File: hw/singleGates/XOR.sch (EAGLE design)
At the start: 15 parts, among them Q1 BC817, Q2 BC817, Q3 BC817, Q4 BC817, Q5 BC817, Q6 BC817

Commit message: Updated gates to be centered
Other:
- moved on the sheet: Q1, Q2, Q3, Q4, Q5, Q6, R1, R2, R3, R4, R5, R6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

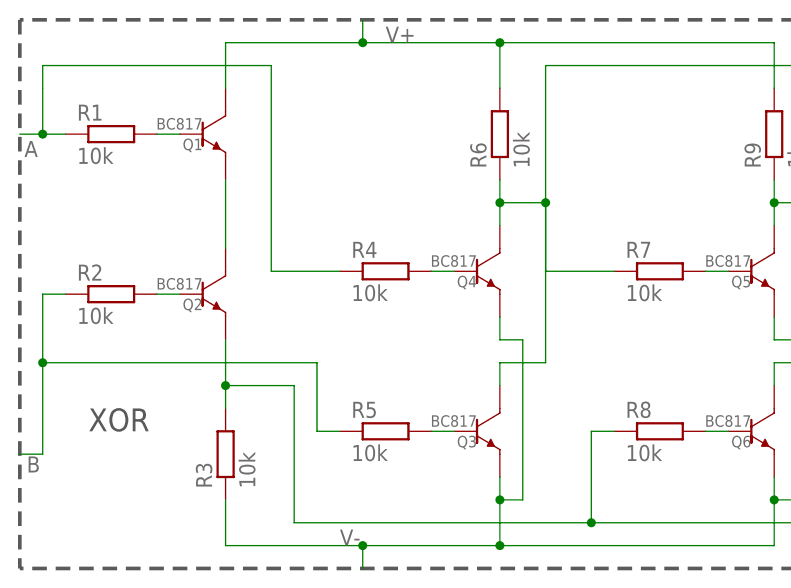
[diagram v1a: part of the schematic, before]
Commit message: Updated supply line names to be more spice compatible
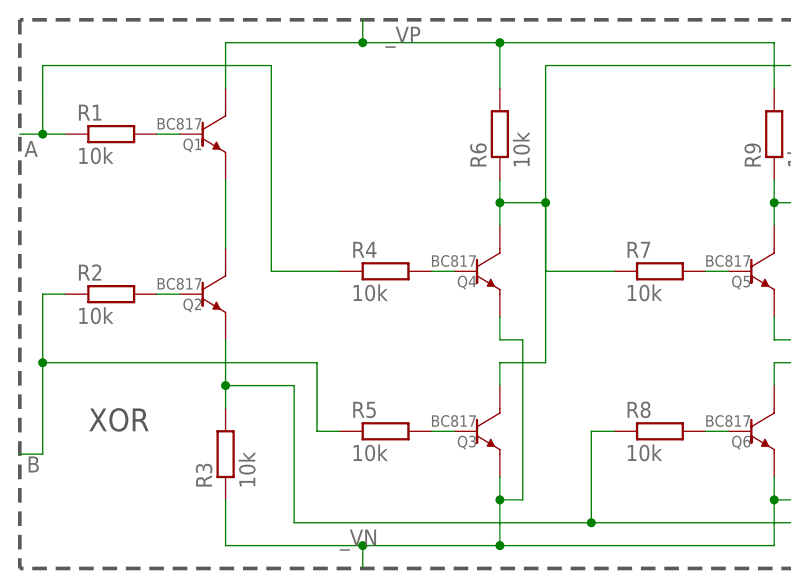
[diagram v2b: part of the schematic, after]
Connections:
- net V+ renamed _VP
- net V- renamed _VN
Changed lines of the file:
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@@
 <?xml version="1.0" encoding="utf-8"?>
 <!DOCTYPE eagle SYSTEM "eagle.dtd">
-<eagle version="7.4.0">
+<eagle version="7.3.0">
 <drawing>
 <settings>
@@
 </busses>
 <nets>
-<net name="V-" class="0">
+<net name="_VN" class="0">
 <segment>
 <wire x1="35.56" y1="-2.54" x2="35.56" y2="-5.08" width="0.1524" layer="91"/>
@@
 </segment>
 </net>
-<net name="V+" class="0">
+<net name="_VP" class="0">
 <segment>
 <wire x1="-25.4" y1="22.86" x2="-25.4" y2="27.94" width="0.1524" layer="91"/>

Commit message: XOR tests
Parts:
- R3, R6: value 10k -> 1k
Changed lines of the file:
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@@
 <?xml version="1.0" encoding="utf-8"?>
 <!DOCTYPE eagle SYSTEM "eagle.dtd">
-<eagle version="7.3.0">
+<eagle version="7.4.0">
 <drawing>
 <settings>
@@
 <part name="R7" library="p.peter-gator" deviceset="R-EU_" device="R0603" value="10k"/>
 <part name="R8" library="p.peter-gator" deviceset="R-EU_" device="R0603" value="10k"/>
-<part name="R3" library="p.peter-gator" deviceset="R-EU_" device="R0603" value="10k"/>
-<part name="R6" library="p.peter-gator" deviceset="R-EU_" device="R0603" value="10k"/>
+<part name="R3" library="p.peter-gator" deviceset="R-EU_" device="R0603" value="1k"/>
+<part name="R6" library="p.peter-gator" deviceset="R-EU_" device="R0603" value="1k"/>
 <part name="R9" library="p.peter-gator" deviceset="R-EU_" device="R0603" value="1k"/>
 <part name="Q1" library="p.peter-gator" deviceset="TRANSISTOR-NPN-GENERIC" device="-SOT23-BEC" technology="DEFAULT" value="BC817"/>
